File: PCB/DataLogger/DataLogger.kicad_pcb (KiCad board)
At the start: 2 copper layers, 59.5 x 49 mm, 23 parts, among them J1 Power, U2 DS18B20, U3 DS18B20, U4 DS18B20, U5 SHT30-DIS

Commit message: Ordered Board
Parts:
- removed U2, U3, U4: DS18B20, ESP32Board:Screw Terminal 3*2.54 1WI
- removed U5: SHT30-DIS, ESP32Board:Screw Terminal 4*2.54 SHT30
- added J10: Screw_Terminal_01x02, ESP32Board:Screw Terminal 2*2.54, F.Cu at (128.1, 114.8)
- added J2: 1WI Screw_Terminal_01x03, ESP32Board:Screw Terminal 3*2.54 1WI, F.Cu at (146.0, 114.8)
- added J3: 1WI Screw_Terminal_01x03, ESP32Board:Screw Terminal 3*2.54 1WI, F.Cu at (154.5, 114.8)
- added J4: 1WI Screw_Terminal_01x03, ESP32Board:Screw Terminal 3*2.54 1WI, F.Cu at (137.5, 114.8)
- added J5: I²C_Screw_Terminal_01x04, ESP32Board:Screw Terminal 4*2.54 I²C, F.Cu at (134.0, 148.1)
- added J6: I²C_Screw_Terminal_01x04, ESP32Board:Screw Terminal 4*2.54 I²C, F.Cu at (145.7, 148.1)
- added J7: Screw_Terminal_01x04, ESP32Board:Screw Terminal 4*2.54, F.Cu at (122.8, 148.1)
- added J8: Screw_Terminal_01x02, ESP32Board:Screw Terminal 2*2.54, F.Cu at (112.4, 114.8)
- added J9: Screw_Terminal_01x02, ESP32Board:Screw Terminal 2*2.54, F.Cu at (107.1, 148.1)
- added JP5: SolderJumper_3_Bridged12, Jumper:SolderJumper-3_P1.3mm_Bridged12_RoundedPad1.0x1.5mm_NumberLabels, F.Cu at (132.4, 132.8)
- added JP6: SolderJumper_3_Bridged12, Jumper:SolderJumper-3_P1.3mm_Bridged12_RoundedPad1.0x1.5mm_NumberLabels, F.Cu at (144.2, 132.8)
- added JP7: SolderJumper_3_Bridged12, Jumper:SolderJumper-3_P1.3mm_Bridged12_RoundedPad1.0x1.5mm_NumberLabels, F.Cu at (121.0, 132.8)
- added JP8: SolderJumper_3_Bridged12, Jumper:SolderJumper-3_P1.3mm_Bridged12_RoundedPad1.0x1.5mm_NumberLabels, F.Cu at (134.0, 136.1)
- added JP9: SolderJumper_3_Bridged12, Jumper:SolderJumper-3_P1.3mm_Bridged12_RoundedPad1.0x1.5mm_NumberLabels, F.Cu at (117.5, 136.1)
- added TP5: 01, TestPoint:TestPoint_THTPad_D1.5mm_Drill0.7mm, F.Cu at (159.4, 118.1)
- added TP6: 05, TestPoint:TestPoint_THTPad_D1.5mm_Drill0.7mm, F.Cu at (161.9, 118.1)
- moved TP1 54.3 mm to (161.9, 120.7), turned to -90 degrees
- moved TP3 52.4 mm to (161.9, 123.2), turned to -90 degrees
- moved TP2 51.4 mm to (159.4, 120.7), turned to -90 degrees
- moved TP4 49.3 mm to (159.4, 123.2), turned to -90 degrees
- moved R9 19.5 mm to (145.9, 136.0)
- moved R1 14.9 mm to (140.2, 129.8)
- moved R2 14.9 mm to (128.7, 129.8)
- moved R3 14.9 mm to (117.2, 129.8)
- moved JP3 14.9 mm to (118.5, 126.3)
- moved JP1 14.9 mm to (142.0, 126.3)
- moved JP2 14.9 mm to (130.3, 126.3)
- moved JP4 13.1 mm to (150.1, 137.5), turned to 90 degrees
- moved R10 11.5 mm to (121.8, 136.1)
- moved J1 0.30 mm to (159.9, 141.7)
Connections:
- JP1 pad 2: Net-(JP1-C) -> Net-(J2-VDD)
- JP2 pad 2: Net-(JP2-C) -> Net-(J3-VDD)
- JP3 pad 2: Net-(JP3-C) -> Net-(J4-VDD)
- JP4 pad 2: Net-(JP4-C) -> Net-(J5-VDD)
- R1 pad 2: Net-(JP1-C) -> Net-(JP5-C)
- R10 pad 1: Net-(JP4-C) -> Net-(JP9-C)
- R2 pad 1: Net-(U1-16) -> Net-(JP6-C)
- R2 pad 2: Net-(JP2-C) -> Net-(J3-Data)
- R3 pad 1: Net-(U1-15) -> Net-(JP7-C)
- R3 pad 2: Net-(JP3-C) -> Net-(J4-Data)
- R9 pad 2: Net-(JP4-C) -> Net-(JP8-C)
- U1 pad 10: unconnected-(U1-26-Pad10) -> Net-(J10-Pin_2)
- U1 pad 23: Net-(U1-15) -> Net-(J7-Pin_4)
- U1 pad 24: unconnected-(U1-2-Pad24) -> Net-(J7-Pin_3)
- U1 pad 25: unconnected-(U1-0-Pad25) -> Net-(J7-Pin_2)
- U1 pad 26: unconnected-(U1-4-Pad26) -> Net-(J7-Pin_1)
- U1 pad 27: Net-(U1-16) -> Net-(J3-Data)
- U1 pad 29: unconnected-(U1-5-Pad29) -> Net-(U1-5)
- U1 pad 30: unconnected-(U1-18-Pad30) -> Net-(J4-Data)
- U1 pad 35: unconnected-(U1-1-Pad35) -> Net-(U1-1)
- U1 pad 9: unconnected-(U1-25-Pad9) -> Net-(J10-Pin_1)
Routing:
- net Net-(J5-VDD): track 0.00 -> 57.6 mm, vias 0 -> 4
- net Net-(J7-Pin_4): track 0.00 -> 51.1 mm
- net Net-(U1-1): track 0.00 -> 45.3 mm, vias 0 -> 2
- net +3V3: track 123.9 -> 85.0 mm, vias 4 -> 0
- net Net-(U1-15): track 37.8 -> 0.00 mm, vias 1 -> 0
- net Net-(U1-5): track 0.00 -> 34.8 mm
- net Net-(J3-VDD): track 0.00 -> 34.2 mm, vias 0 -> 3
- net Net-(J7-Pin_3): track 0.00 -> 34.1 mm
- net Net-(J7-Pin_1): track 0.00 -> 33.9 mm
- net Net-(J7-Pin_2): track 0.00 -> 33.7 mm
- net Net-(JP4-C): track 33.3 -> 0.00 mm
- net Net-(J2-VDD): track 0.00 -> 32.1 mm, vias 0 -> 2
- net Net-(J10-Pin_2): track 0.00 -> 31.1 mm, vias 0 -> 1
- net Net-(J10-Pin_1): track 0.00 -> 31.0 mm, vias 0 -> 1
- net Net-(J3-Data): track 0.00 -> 28.4 mm
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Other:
- board size 59.5 x 49 mm -> 59.5 x 46 mm
- board text added: "IO00"
- board text added: "IO02"
- board text added: "IO04"
- board text added: "IO18"
- board text added: "IO25"
- board text added: "IO26"

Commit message: PCB V1.2
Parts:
- removed J1: Power, ESP32Board:Screw Terminal 2*2.54 Power
- removed J4: 1WI Screw_Terminal_01x03, ESP32Board:Screw Terminal 3*2.54 1WI
- removed J5, J6: I²C_Screw_Terminal_01x04, ESP32Board:Screw Terminal 4*2.54 I²C
- removed the REF** at (118.0, 111.8)
- removed the REF** at (118.0, 151.8)
- removed the REF** at (162.5, 151.8)
- removed the REF** at (162.5, 111.8)
- added 1WI3: 1WI Screw_Terminal_01x03, ESP32Board:Screw Terminal 3*2.54 1WI, F.Cu at (146.5, 145.8)
- added I²C1: I²C_Screw_Terminal_01x04, ESP32Board:Screw Terminal 4*2.54 I²C, F.Cu at (143.1, 112.1)
- added I²C2: I²C_Screw_Terminal_01x04, ESP32Board:Screw Terminal 4*2.54 I²C, F.Cu at (132.1, 112.1)
- added Power1: Power, ESP32Board:Screw Terminal 2*2.54 Power, F.Cu at (159.2, 142.3)
- added R4: 4k7, Resistor_THT:R_Axial_DIN0207_L6.3mm_D2.5mm_P7.62mm_Horizontal, F.Cu at (106.4, 113.8)
- added REF**: MountingHole_4.3mm_M4_ISO14580, MountingHole:MountingHole_4.3mm_M4_ISO14580, F.Cu at (162.5, 105.8)
- added REF**: MountingHole_4.3mm_M4_ISO14580, MountingHole:MountingHole_4.3mm_M4_ISO14580, F.Cu at (162.5, 151.8)
- added REF**: MountingHole_4.3mm_M4_ISO14580, MountingHole:MountingHole_4.3mm_M4_ISO14580, F.Cu at (118.0, 151.8)
- added REF**: MountingHole_4.3mm_M4_ISO14580, MountingHole:MountingHole_4.3mm_M4_ISO14580, F.Cu at (118.0, 105.8)
- added U2: DS18B20, Package_TO_SOT_THT:TO-92_Inline, F.Cu at (119.2, 112.8)
- ExtraGPIO2: renamed from J10; value Screw_Terminal_01x02 -> Screw_Terminal_01x
- R1, R10, R2, R3, R9: value 1k5 -> 2k2
- TP3: value 3.3V -> 3V3
- TP4: value RESET -> EN
- moved TP1 56.6 mm to (107.2, 106.2), turned to 0 degrees
- moved TP4 54.2 mm to (107.2, 108.8), turned to 0 degrees
- moved TP6 53.0 mm to (109.7, 108.8), turned to 180 degrees
- moved TP3 52.5 mm to (112.2, 106.2), turned to 0 degrees
- moved TP2 51.7 mm to (109.7, 106.2), turned to 0 degrees
- moved TP5 48.1 mm to (112.2, 108.8), turned to 180 degrees
- moved ExtraGPIO1 47.8 mm to (154.2, 112.1), turned to 90 degrees
- moved J8 46.4 mm to (158.8, 115.6), turned to 0 degrees
- moved 1WI2 39.7 mm to (129.6, 145.8), turned to -90 degrees
- moved JP9 36.9 mm to (152.6, 124.8), turned to 180 degrees
- moved JP4 33.2 mm to (119.3, 124.9), turned to 0 degrees
- moved 1WI1 32.0 mm to (138.0, 145.8), turned to -90 degrees
- moved ExtraGPIO2 31.3 mm to (123.8, 145.8), turned to -90 degrees
- moved R3 30.9 mm to (147.7, 134.8)
- moved JP7 30.9 mm to (151.5, 127.8)
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- renumbered J2 to 1WI1, J3 to 1WI2, J7 to ExtraGPIO1
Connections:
- net Net-(J10-Pin_1) renamed /IO25
- net Net-(J10-Pin_2) renamed /IO26
- net Net-(J2-Data) renamed /IO17
- net Net-(J3-Data) renamed /IO16
- net Net-(J4-Data) renamed /IO18
- net Net-(J7-Pin_4) renamed /IO15
- net Net-(U1-1) renamed /IO01
- net Net-(U1-5) renamed /IO05
- net Net-(U1-RESET) renamed /RESET
- ExtraGPIO1 pad 1: Net-(J7-Pin_1) -> /IO00
- ExtraGPIO1 pad 2: Net-(J7-Pin_2) -> /IO02
- ExtraGPIO1 pad 3: Net-(J7-Pin_3) -> /IO04
- U1 pad 15: unconnected-(U1-13-Pad15) -> /IO13
- U1 pad 24: Net-(J7-Pin_3) -> /IO02
- U1 pad 25: Net-(J7-Pin_2) -> /IO00
- U1 pad 26: Net-(J7-Pin_1) -> /IO04
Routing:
- net +5V: track 55.5 -> 0.00 mm, vias 16 -> 0
- net /IO13: track 0.00 -> 53.9 mm, vias 0 -> 2
- net /IO15: track 51.1 -> 5.62 mm
- net /IO01: track 45.3 -> 10.0 mm, vias 2 -> 0
- net /IO18: track 19.6 -> 54.3 mm, vias 1 -> 0
- net Net-(J7-Pin_3): track 34.1 -> 0.00 mm
- net Net-(J7-Pin_1): track 33.9 -> 0.00 mm
- net Net-(J7-Pin_2): track 33.7 -> 0.00 mm
- net Net-(I²C1-SCL): track 66.8 -> 40.4 mm, vias 3 -> 0
- net /IO26: track 31.1 -> 6.54 mm, vias 1 -> 0
- net /IO25: track 31.0 -> 6.54 mm, vias 1 -> 0
- net /RESET: track 59.1 -> 39.0 mm
- net GND: track 34.9 -> 17.3 mm, vias 11 -> 10
- net /IO00: track 0.00 -> 14.6 mm
- net Net-(1WI2-VDD): track 34.2 -> 21.9 mm, vias 3 -> 0
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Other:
- board size 59.5 x 46 mm -> 59.5 x 52 mm
- board text added: "Datalogger V1.2"
- board text added: "I²C"
- board text added: "locked"
- board text removed: "Datalogger V1"

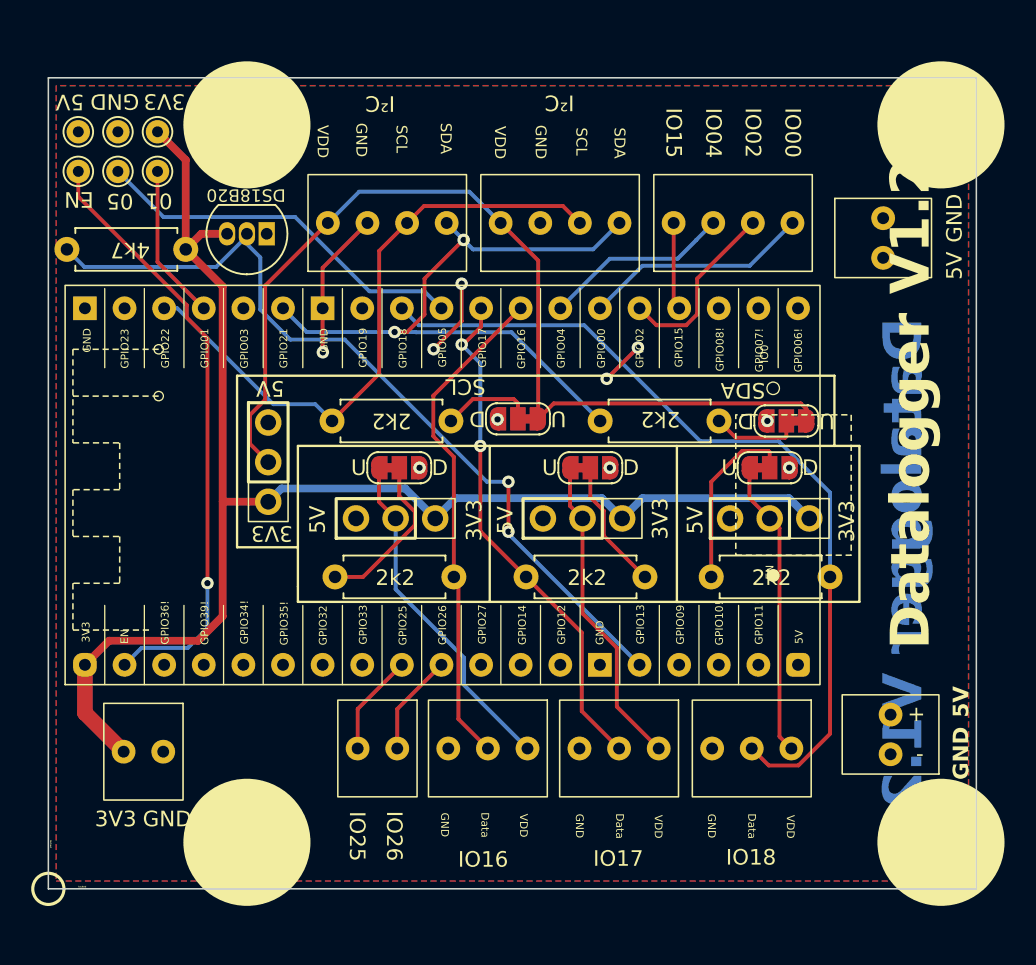
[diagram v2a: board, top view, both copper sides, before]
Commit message: Add voltage devider to measure supply voltage
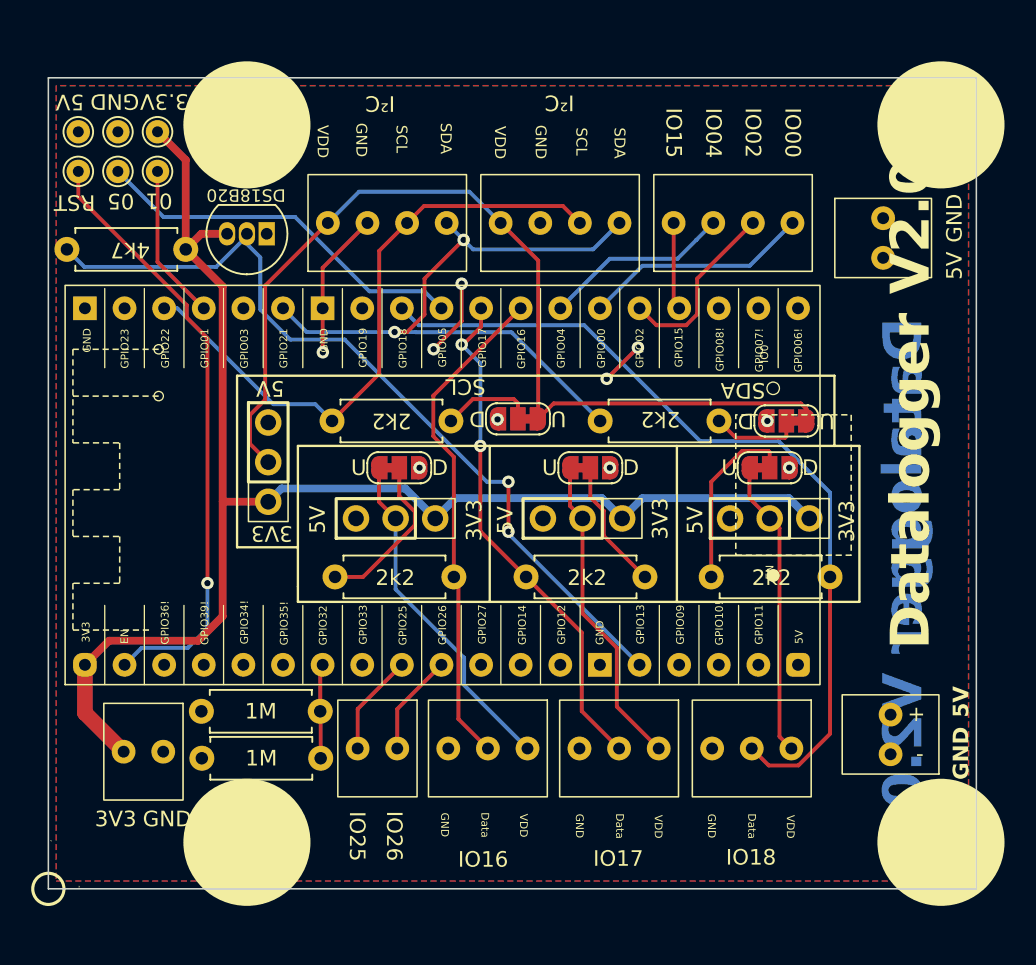
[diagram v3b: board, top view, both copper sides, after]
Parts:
- added R5: 1M, Resistor_THT:R_Axial_DIN0207_L6.3mm_D2.5mm_P7.62mm_Horizontal, F.Cu at (122.7, 143.4)
- added R6: 1M, Resistor_THT:R_Axial_DIN0207_L6.3mm_D2.5mm_P7.62mm_Horizontal, F.Cu at (115.1, 146.4)
- TP3: value 3V3 -> 3.3V
- TP4: value EN -> RST
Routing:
- net unconnected-(R5-Pad1): track 0.00 -> 6.07 mm
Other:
- board text added: "Datalogger V2.0"
- board text added: "X"
- board text added: "Y"
- board text removed: "Datalogger V1.2"
- board text removed: "locked"
